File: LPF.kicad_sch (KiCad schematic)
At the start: 24 parts

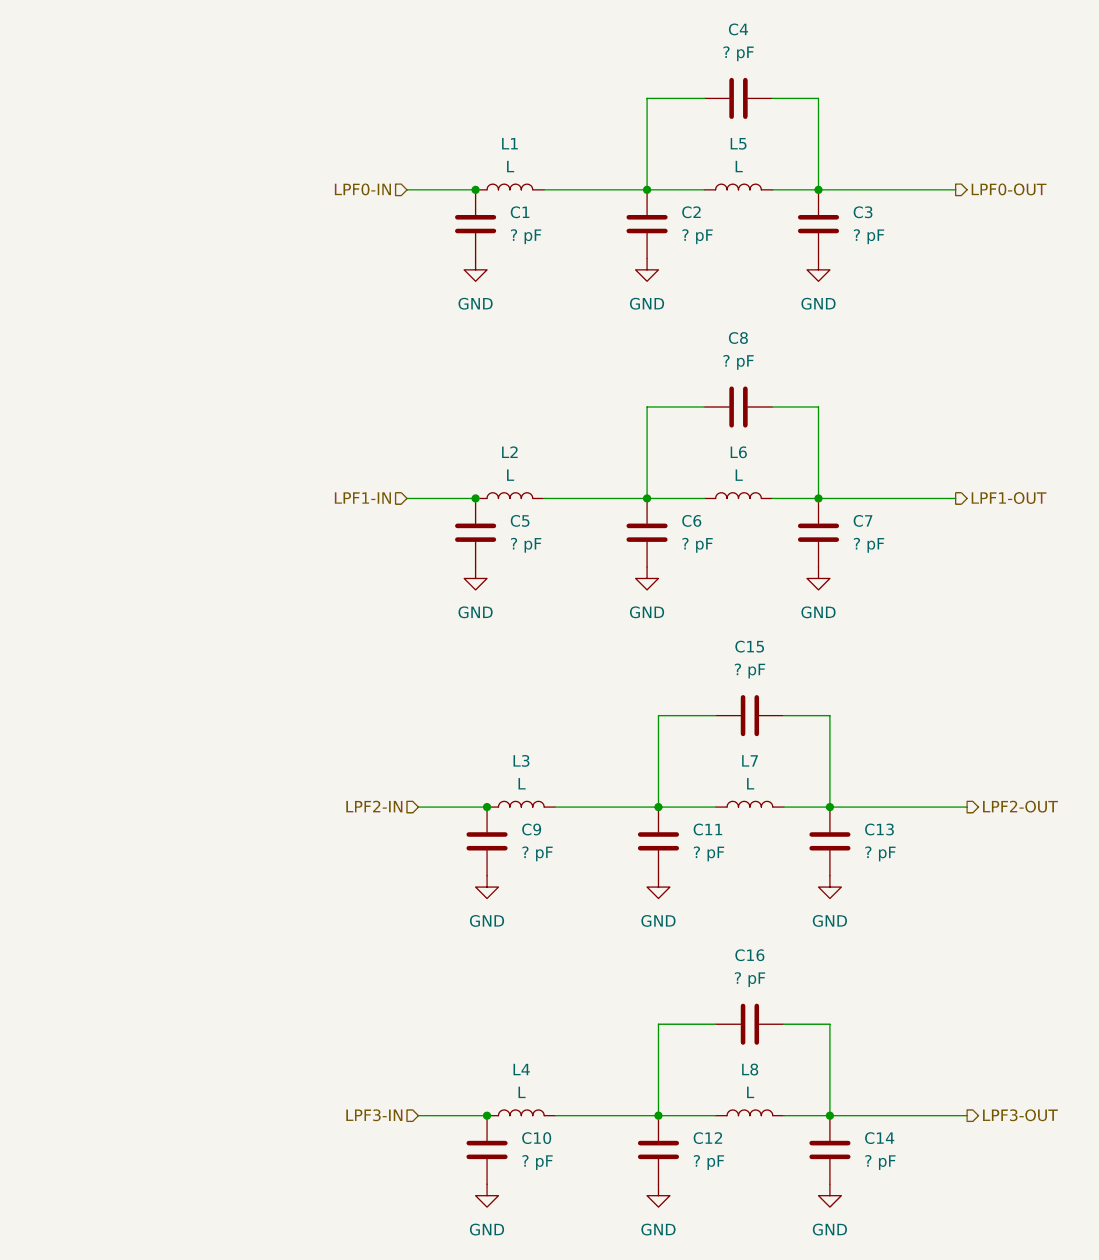
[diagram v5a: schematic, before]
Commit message: added cap values to filter chain per Ron
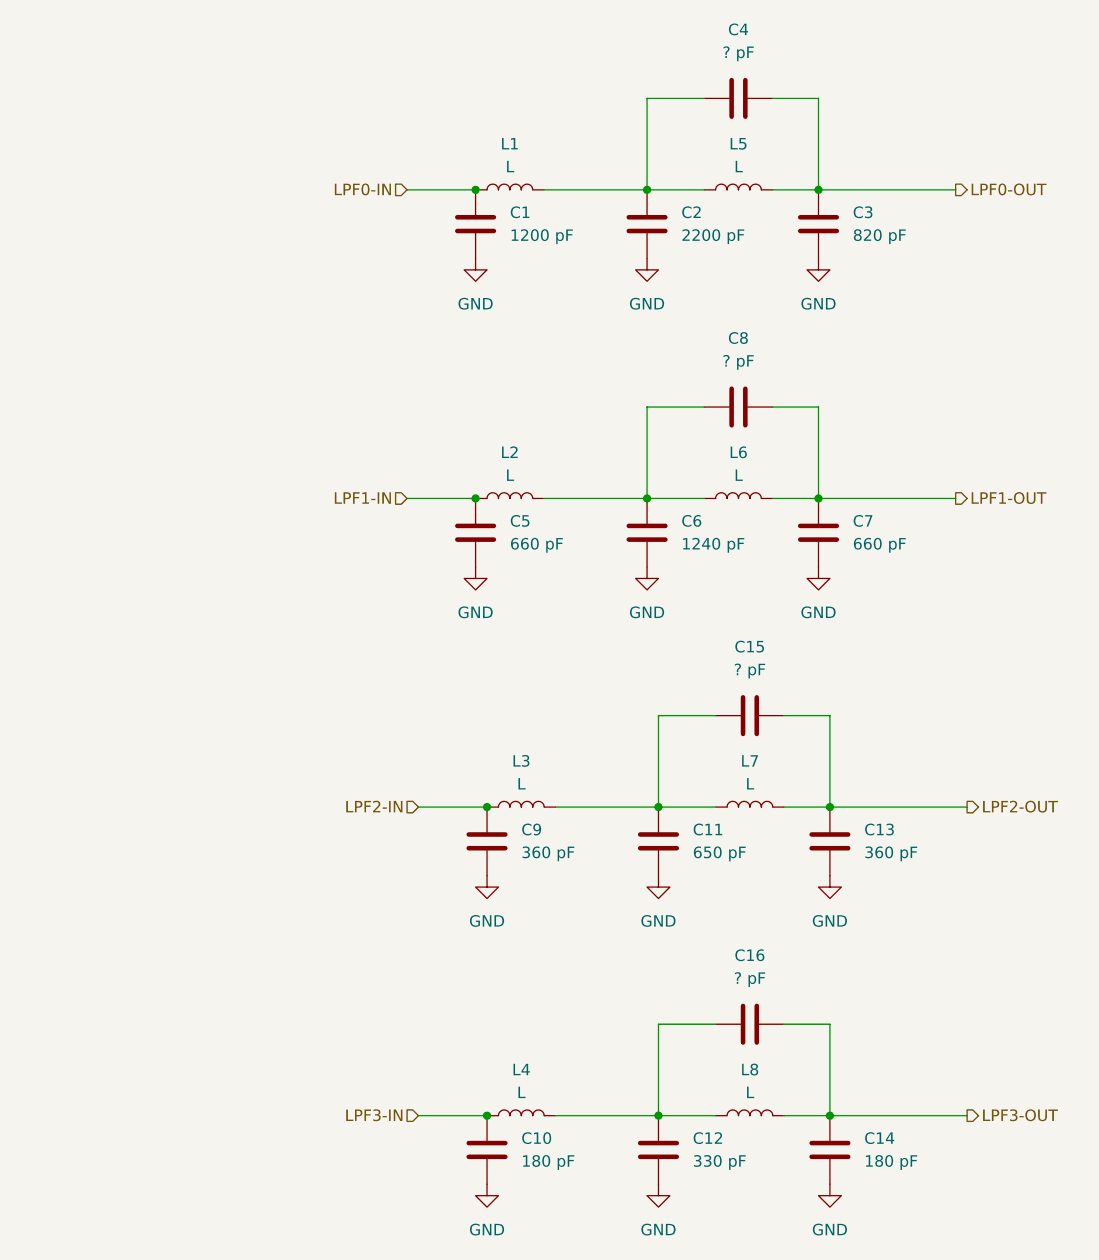
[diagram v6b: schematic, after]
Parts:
- C1: value ? pF -> 1200 pF
- C10, C14: value ? pF -> 180 pF
- C11: value ? pF -> 650 pF
- C12: value ? pF -> 330 pF
- C13, C9: value ? pF -> 360 pF
- C2: value ? pF -> 2200 pF
- C3: value ? pF -> 820 pF
- C5, C7: value ? pF -> 660 pF
- C6: value ? pF -> 1240 pF
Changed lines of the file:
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@@
 	(title_block
 		(title "QMX Amp")
-		(date "2024-08-10")
+		(date "2024-08-11")
 		(rev "v0.2")
 		(company "WA7GIL")
@@
 			)
 		)
-		(property "Value" "? pF"
+		(property "Value" "1200 pF"
 			(at 104.14 46.9899 0)
 			(effects
@@
 			)
 		)
-		(property "Value" "? pF"
+		(property "Value" "820 pF"
 			(at 142.24 46.9899 0)
 			(effects
@@
 			)
 		)
-		(property "Value" "? pF"
+		(property "Value" "330 pF"
 			(at 124.46 149.8599 0)
 			(effects
@@
 			)
 		)
-		(property "Value" "? pF"
+		(property "Value" "180 pF"
 			(at 105.41 149.8599 0)
 			(effects
@@
 			)
 		)
-		(property "Value" "? pF"
+		(property "Value" "650 pF"
 			(at 124.46 115.5699 0)
 			(effects
@@
 			)
 		)
-		(property "Value" "? pF"
+		(property "Value" "2200 pF"
 			(at 123.19 46.9899 0)
 			(effects
@@
 			)
 		)
-		(property "Value" "? pF"
+		(property "Value" "360 pF"
 			(at 105.41 115.5699 0)
 			(effects
@@
 			)
 		)
-		(property "Value" "? pF"
+		(property "Value" "180 pF"
 			(at 143.51 149.8599 0)
 			(effects
@@
 			)
 		)
-		(property "Value" "? pF"
+		(property "Value" "660 pF"
 			(at 104.14 81.2799 0)
 			(effects
@@
 			)
 		)
-		(property "Value" "? pF"
+		(property "Value" "660 pF"
 			(at 142.24 81.2799 0)
 			(effects
@@
 			)
 		)
-		(property "Value" "? pF"
+		(property "Value" "1240 pF"
 			(at 123.19 81.2799 0)
 			(effects
@@
 			)
 		)
-		(property "Value" "? pF"
+		(property "Value" "360 pF"
 			(at 143.51 115.5699 0)
 			(effects
